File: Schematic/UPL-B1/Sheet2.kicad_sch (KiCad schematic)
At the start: 0 parts

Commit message: Begin drawing IMD section
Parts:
- added IC1: DAC8143FSZ, SOIC127P1032X265-16N, symbol UPL_B1:DAC8143FSZ
- added K1, K2: SILxx-1Cxx-51x, Relay_THT:Relay_SPDT_StandexMeder_SIL_Form1C, symbol Relay:SILxx-1Cxx-51x
- added R1: 47R5, symbol Device:R
- added U1: NE5534, symbol Amplifier_Operational:NE5534
- added V2: BC850B, Package_TO_SOT_SMD:SOT-23, symbol Transistor_BJT:BC850
- added X2: Conn_01x03_Pin_Bridge, Connector_PinHeader_2.54mm:PinHeader_1x03_P2.54mm_Vertical, symbol UPL_B1:Conn_01x03_Pin_Bridge
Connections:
- new net: K2.1, R1.2
- new net: K1.1, R1.1, X2.2 (Pin_2)
- new net: IC1.1 (IOUT1), U1.2 (-)
- new net: IC1.15 (VREF), K1.7
- new net: K1.5, V2.3 (C)
- new net COS: X2.1 (Pin_1)
- new net GND: IC1.2 (IOUT2), IC1.3 (AGND), K1.2, X2.3 (Pin_3)

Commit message: update on Output IMD
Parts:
- removed V2: BC850B, Package_TO_SOT_SMD:SOT-23, symbol Transistor_BJT:BC850
- added C200, C201, C202, C203, C204, C205: 100uF 25V, symbol Device:C_Polarized_Small
- added C206, C207, C209: 100nF, symbol Device:C_Small
- added D20, U2: 74HC86, symbol 74xx:74HC86
- added D21: 74HCT4094D,118, 74HCT4094D118, symbol UPL_B1:74HCT4094D,118
- added P20: TestPoint, symbol Connector:TestPoint
- added R200, R201, R202: 10K, symbol Device:R_Small
- added R203, R204, R205: 10, symbol Device:R_Small
- added R206, R207: 1K, symbol Device:R_Small
- added V20: BAS32, Diode_SMD:D_SOD-523, symbol Diode:1N4148WT
- added V21: BC850B, Package_TO_SOT_SMD:SOT-23, symbol Transistor_BJT:BC850
- renumbered IC1 to D22, K1 to K2, R1 to R215
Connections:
- net +5V: now reaches K2.3
- net +5V: now also C200.1, C205.1, C207.1, C209.1, D21.16 (VCC), R200.1, R205.1, R205.2, R206.1, V20.1 (K)
- net at K2.5: now also V20.2 (A), V21.3 (C)
- net GND renamed GNDD
- net GNDD: now also C200.2, C201.2, C202.1, C203.2, C204.1, C205.2, C206.2, C207.2, C209.2, D21.8 (GND), R201.2, R207.1, V21.2 (E)
- new net: D20.1, R206.2
- new net: D20.12, D20.5, D20.9, R207.2
- new net: R202.2, V21.1 (B)
- new net: D21.4 (QP0), R202.1
- new net +15V: C201.1, C203.1, R203.1, R203.2
- new net +2V5: C206.1, P20.1, R200.2, R201.1
- new net -15V: C202.2, R204.1
- new net 15V: C204.2, R204.2
- new net CLK: D20.10, D20.8, D21.3 (CP)
- new net ENABLE: D21.15 (OE)
- new net FILT: D21.7 (QP3)
- new net FREQ_ENA: D21.11 (QP7)
- new net LOFILT: D21.6 (QP2)
- new net SDI: D21.10 (QS2), D21.2 (D)
- new net WR: D20.3, D21.1 (STR)
- new net ~{RD}: D20.11, D20.13
- new net ~{WR}: D20.2, D20.4, D20.6
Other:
- note added: "BOARD ID"
- note added: "DATA LINK"
- note added: "IMD ATTEN"
- moved on the sheet: D22, K2, R215, U1, X2

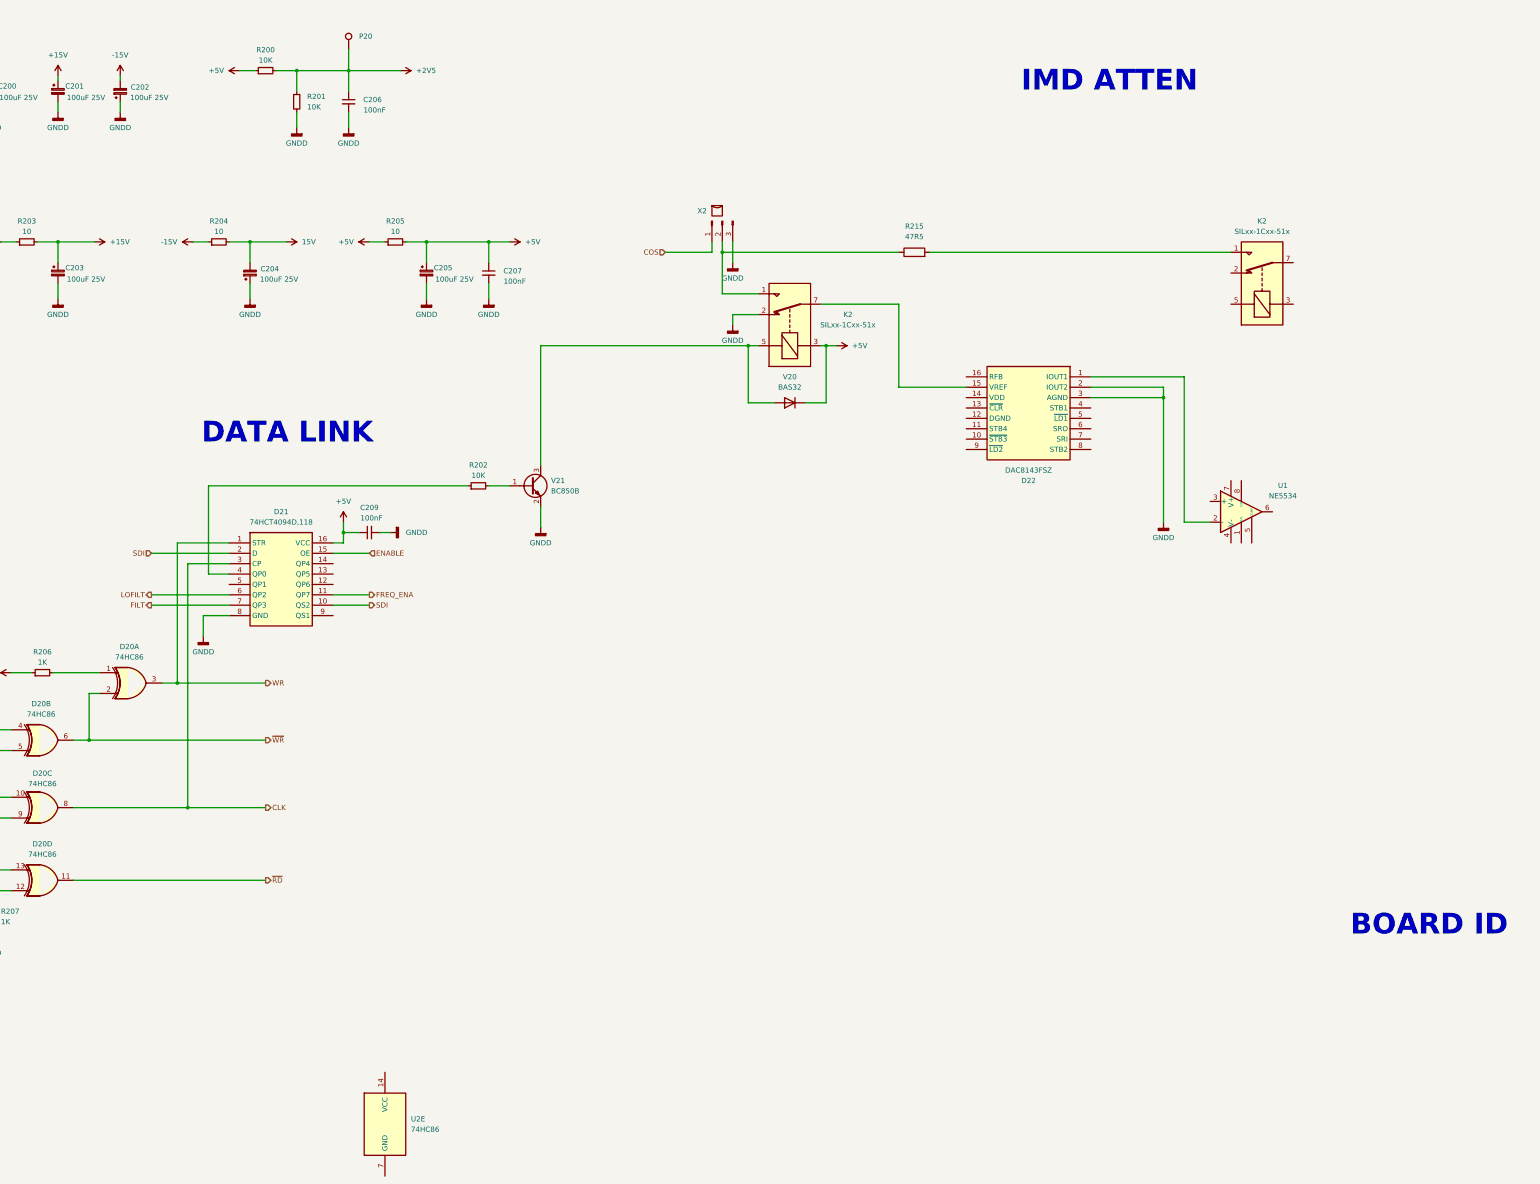
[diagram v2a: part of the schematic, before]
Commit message: IMD Atten added
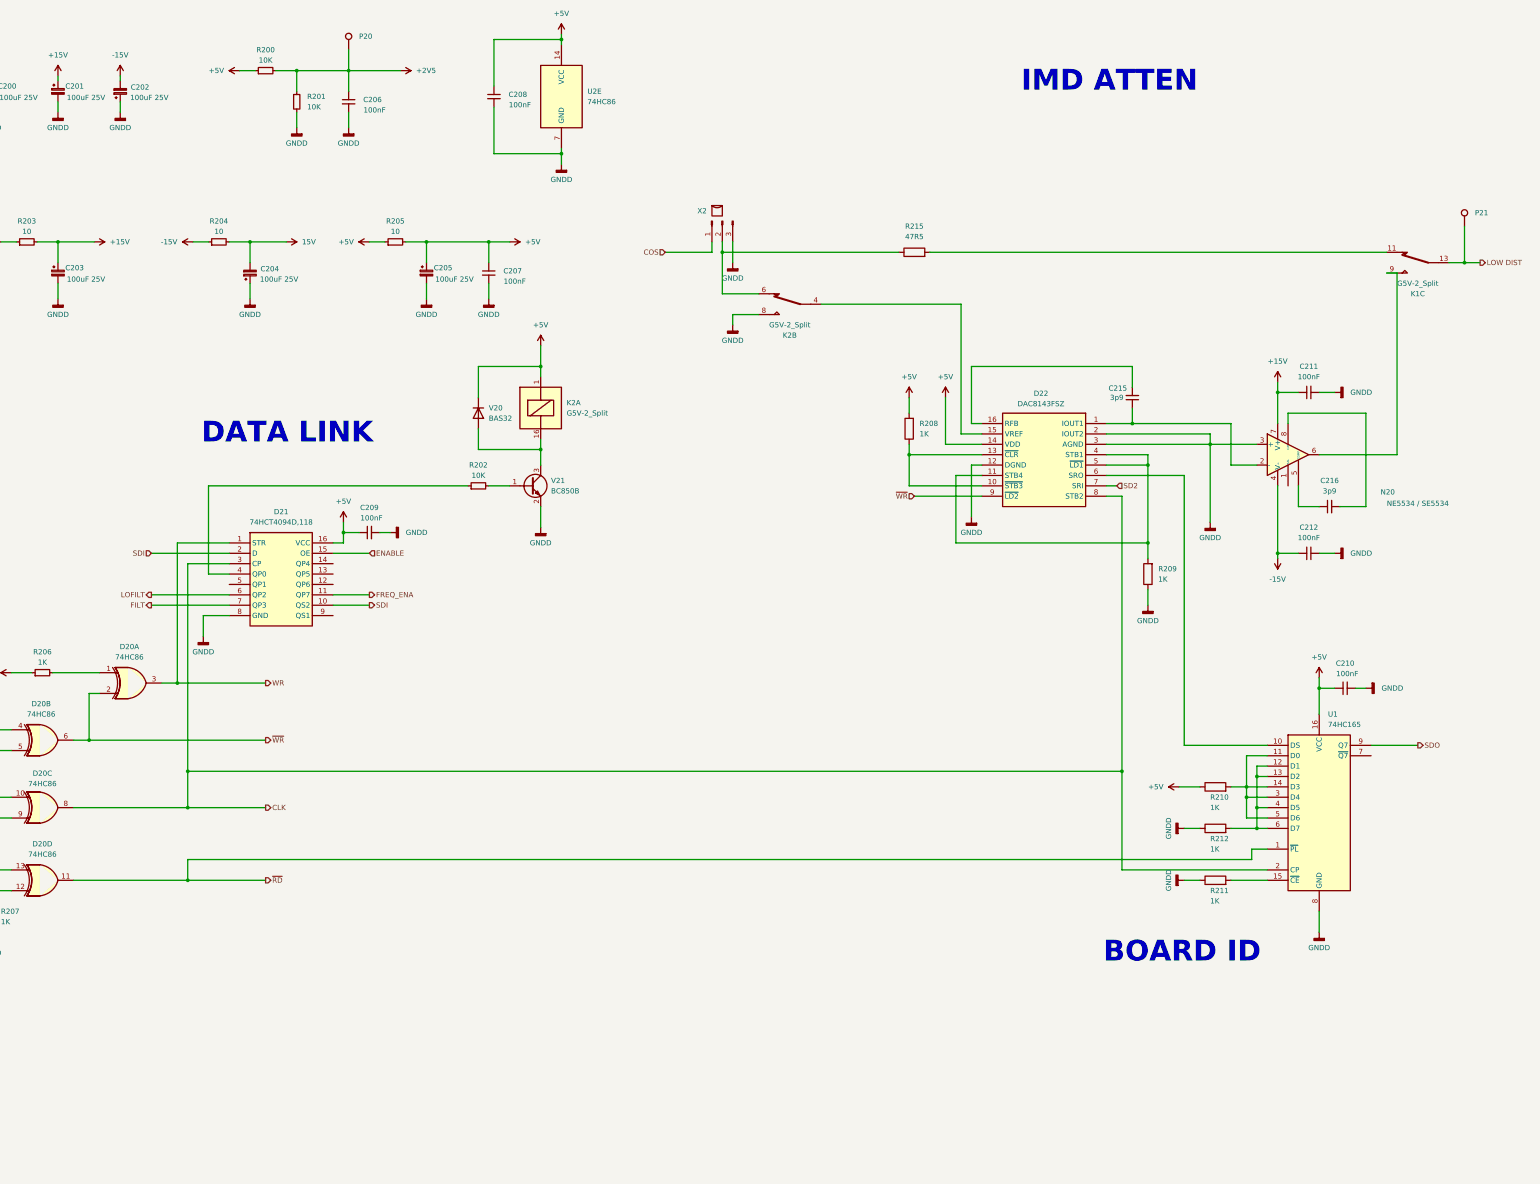
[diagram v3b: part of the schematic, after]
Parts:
- removed K2 (x2): SILxx-1Cxx-51x, Relay_THT:Relay_SPDT_StandexMeder_SIL_Form1C, symbol Relay:SILxx-1Cxx-51x
- removed U1: NE5534, symbol Amplifier_Operational:NE5534
- added C208, C210, C211, C212: 100nF, symbol Device:C_Small
- added C215, C216: 3p9, symbol Device:C_Small
- added K1, K2: G5V-2_Split, Relay_THT:Relay_DPDT_Omron_G5V-2, symbol Relay:G5V-2_Split
- added N20: NE5534 / SE5534, symbol Amplifier_Operational:NE5534
- added P21: TestPoint, symbol Connector:TestPoint
- added R208, R209, R210, R211, R212: 1K, symbol Device:R
- added U1: 74HC165, symbol 74xx:74HC165
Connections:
- net +15V: now also C211.1, N20.7 (V+)
- net +5V: now also D22.14 (VDD), U2.14 (VCC), C208.1, C210.1, K2.1, R208.2, R210.1, U1.16 (VCC)
- net -15V: now also C212.1, N20.4 (V-)
- net CLK: now also D22.8 (STB2), U1.2 (CP)
- net GNDD: now also D22.12 (DGND), U2.7 (GND), C208.2, C210.2, C211.2, C212.2, K2.8, N20.3 (+), R209.1, R211.1, R212.1, U1.8 (GND)
- net ~{RD}: now also U1.1 (~{PL})
- net ~{WR}: now also D22.9 (~{LD2})
- net at V20.2 (A), V21.3 (C): now also K2.16
- net at R215.2: now also K1.11
- net at R215.1, X2.2 (Pin_2): now also K2.6
- net at D22.1 (IOUT1): now also C215.1, N20.2 (-)
- net at D22.10 (~{STB3}): now also D22.13 (~{CLR}), R208.1
- net at D22.11 (STB4): now also D22.4 (STB1), D22.5 (~{LD1}), R209.2
- net at D22.15 (VREF): now also K2.4
- net at D22.16 (RFB): now also C215.2
- net at D22.6 (SRO): now also U1.10 (DS)
- net SD2: now reaches D22.7 (SRI)
- new net: R211.2, U1.15 (~{CE})
- new net: R212.2, U1.12 (D1), U1.13 (D2), U1.4 (D5), U1.6 (D7)
- new net: C216.1, N20.5 (COMP)
- new net: K1.9, N20.6
- new net: C216.2, N20.8 (C/B)
- new net: R210.2, U1.11 (D0), U1.14 (D3), U1.3 (D4), U1.5 (D6)
- new net LOW DIST: K1.13, P21.1
- new net SDO: U1.9 (Q7)
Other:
- moved on the sheet: D22, U2E, V20

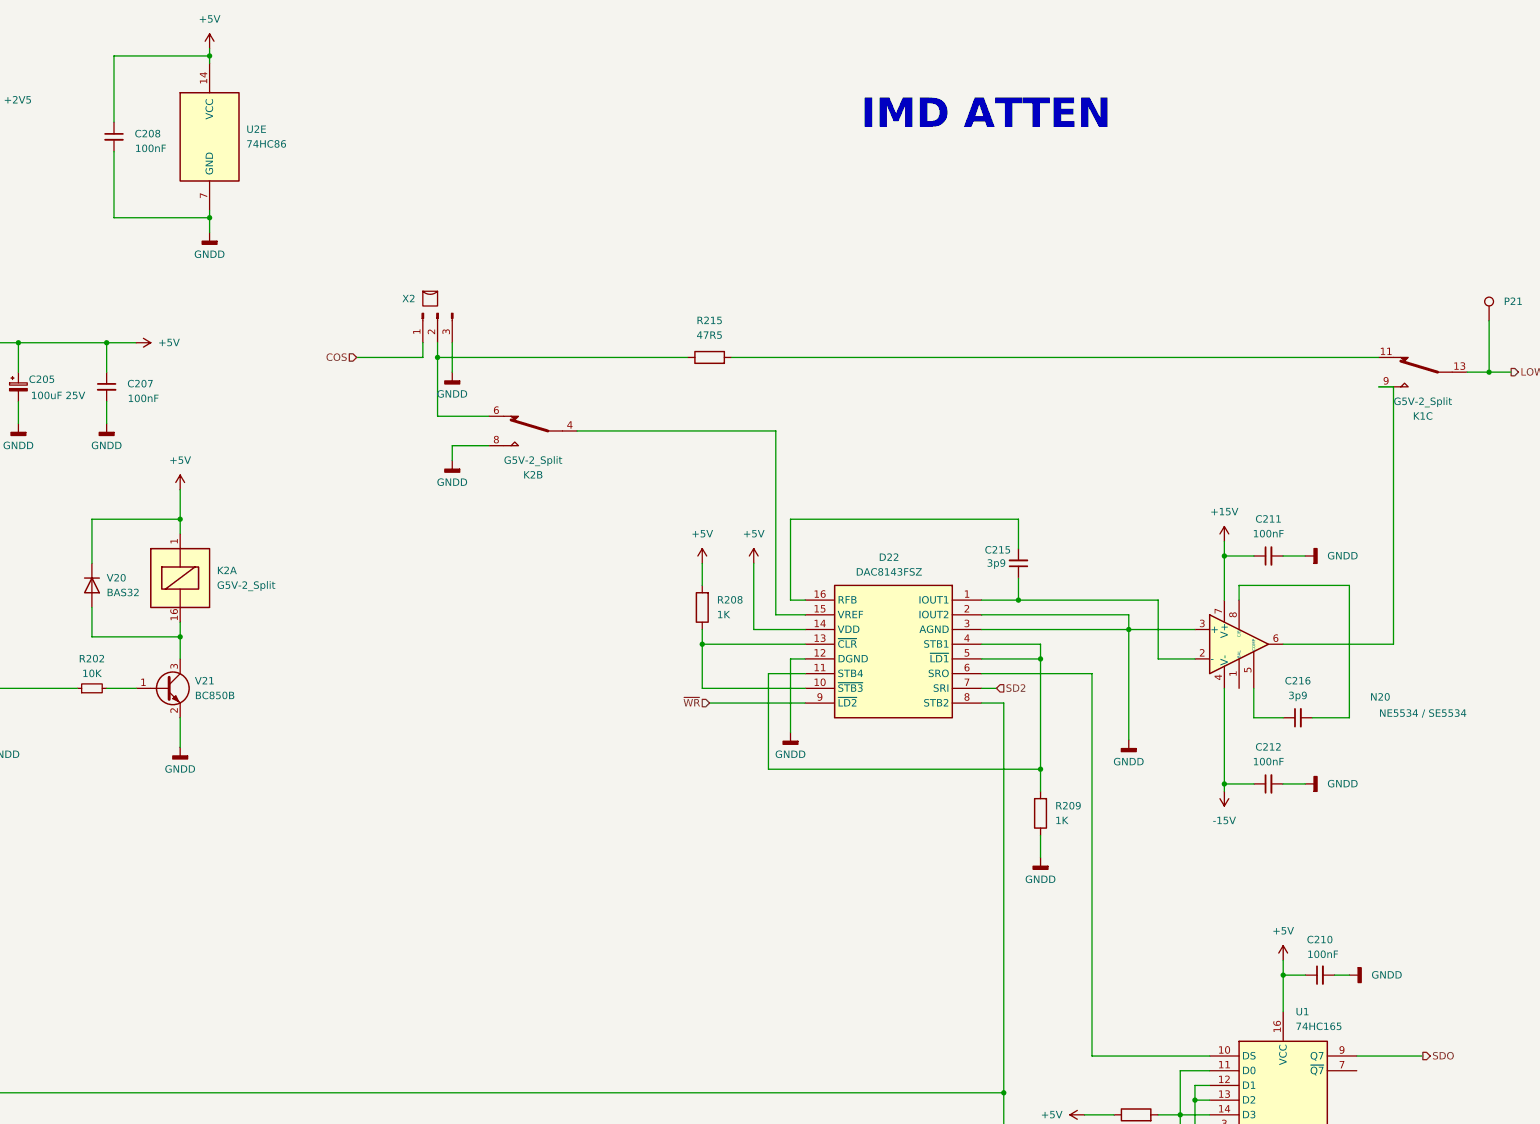
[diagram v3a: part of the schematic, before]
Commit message: Cleanup component names
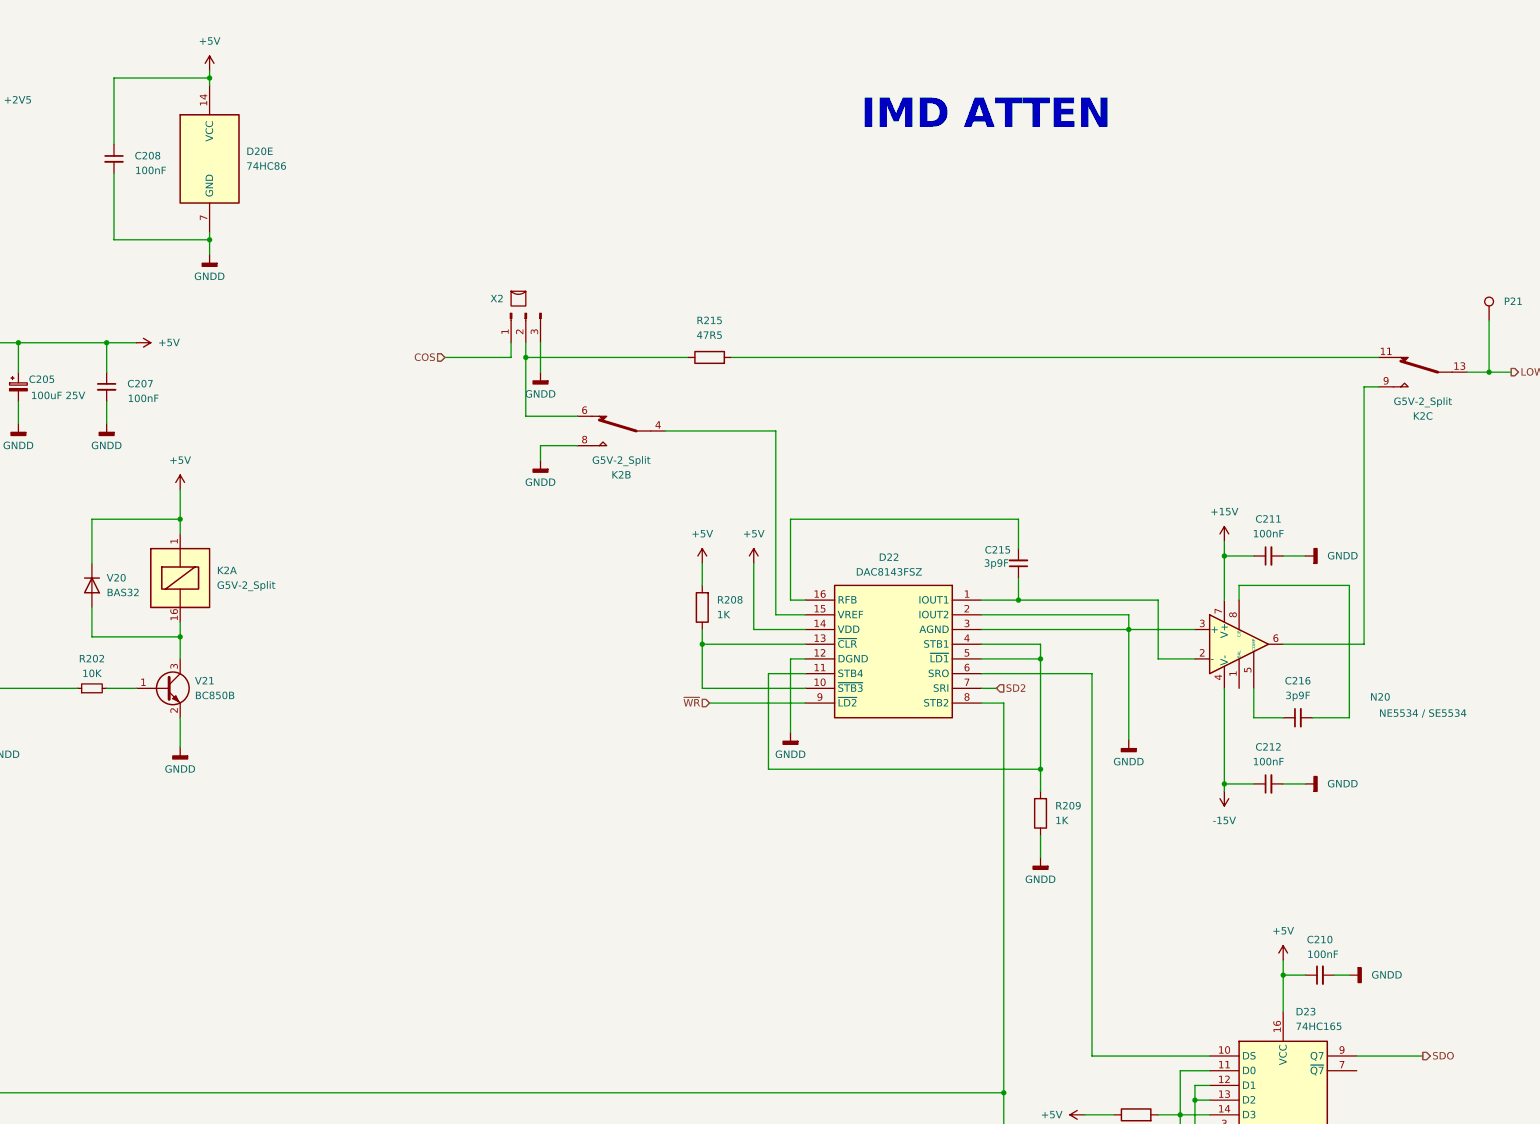
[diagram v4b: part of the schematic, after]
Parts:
- C215, C216: value 3p9 -> 3p9F
- renumbered U2 to D20, U1 to D23, K1 to K2
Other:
- moved on the sheet: C208, D20E, K2B, X2
